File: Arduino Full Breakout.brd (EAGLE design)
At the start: 114.3 x 149.9 mm, 18 parts, among them J1 ARDUINO_R3_SHIELDUNO_R3_SHIEL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

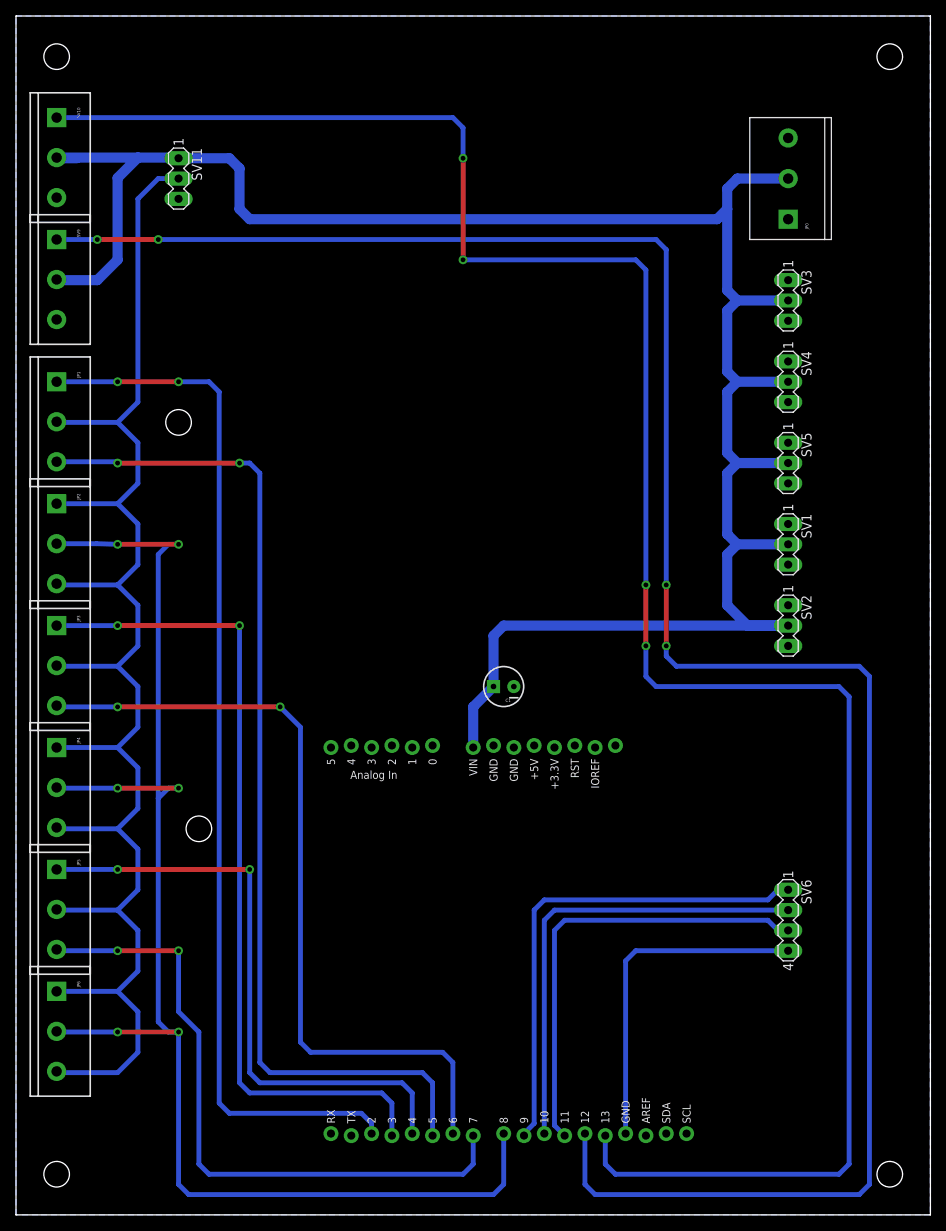
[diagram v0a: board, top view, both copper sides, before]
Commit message: add pushbutton debounce to full size breakout board
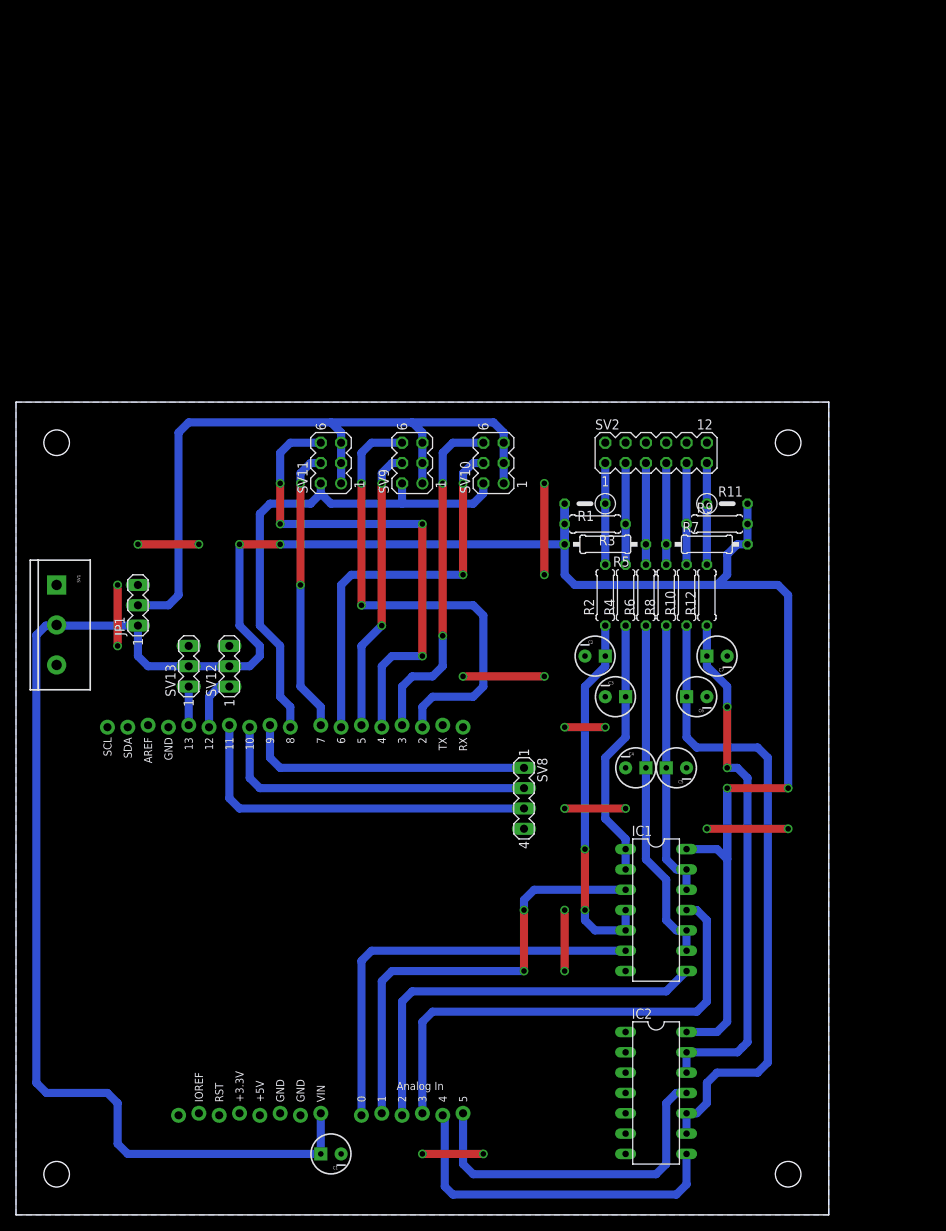
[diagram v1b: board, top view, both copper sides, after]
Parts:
- removed JP0: (no value), MY-Connectors:SCREWTERMINAL-5MM-3
- removed JP2, JP3, JP4, JP5, JP6: (no value), SparkFun-Connectors:SCREWTERMINAL-5MM-3
- removed SV3, SV4, SV5: (no value), con-lstb:MA03-1
- removed SV6: (no value), con-lstb:MA04-1
- added C2, C3, C4, C5, C6, C7: 10uF, SparkFun-Passives:CPOL-RADIAL-10UF-25V
- added IC1, IC2: 74HC00N, 74xx-eu:DIL14
- added R1, R11: 10k, rcl:0207/5V
- added R10, R12, R2, R4, R6, R8: 1k00, rcl:0207/7
- added R3, R9: 10k, rcl:0207/7
- added R5, R7: 10k, rcl:0207/10
- added SV12, SV13: (no value), con-lstb:MA03-1
- added SV8: (no value), con-lstb:MA04-1
- JP1: device SparkFun-Connectors:SCREWTERMINAL-5MM-3 -> con-lstb:MA03-1
- SV1: device con-lstb:MA03-1 -> SparkFun-Connectors:SCREWTERMINAL-5MM-3
- SV10, SV9: device SparkFun-Connectors:SCREWTERMINAL-5MM-3 -> con-lstb:MA03-2
- SV11: device con-lstb:MA03-1 -> con-lstb:MA03-2
- SV2: device con-lstb:MA03-1 -> con-lstb:MA06-2
- moved J1 108.2 mm to (1.27, 63.5), turned to 270 degrees
- moved SV1 91.6 mm to (5.08, 78.7)
- moved SV10 69.6 mm to (59.7, 94.0), turned to 90 degrees
- moved C1 62.3 mm to (39.4, 7.62)
- moved SV9 52.5 mm to (49.5, 94.0), turned to 90 degrees
- moved SV11 40.3 mm to (39.4, 94.0), turned to 90 degrees
- moved JP1 29.7 mm to (15.2, 76.2), turned to 90 degrees
- moved SV2 27.2 mm to (80.0, 95.2), turned to 0 degrees
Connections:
- removed net B0: SV1.1
- removed net B1: SV2.1
- removed net B2: SV3.1
- removed net B4: SV4.1
- removed net B5: SV5.1
- new net BUTTONS3: IC1.11, J1.A3
- new net N$10: C5.1, IC1.12, IC1.13, R8.1
- new net N$11: R7.1, R8.2, SV2.7
- new net N$12: C6.1, IC2.10, IC2.9, R10.1
- new net N$13: R10.2, R9.1, SV2.9
- new net N$16: C7.1, IC2.12, IC2.13, R12.1
- new net N$17: R11.1, R12.2, SV2.11
- new net N$3: C2.1, IC1.4, IC1.5, R2.1
- new net N$4: R1.1, R2.2, SV2.1
- new net N$5: C3.1, IC1.1, IC1.2, R4.1
- new net N$6: R3.1, R4.2, SV2.3
- new net N$7: C4.1, IC1.10, IC1.9, R6.1
- new net N$8: R5.1, R6.2, SV2.5
- net BUTTONS0: now also IC1.6
- net BUTTONS1: now also IC1.3
- net BUTTONS2: now also IC1.8
- net BUTTONS4: now also IC2.8
- net BUTTONS5: now also IC2.11
- net GND: now also C2.2, C3.2, C4.2, C5.2, C6.2, C7.2, IC1.7, IC2.1, IC2.2, IC2.4, IC2.5, IC2.7, JP1.3, SV12.3, SV13.3, SV2.10, SV2.12, SV2.2, SV2.4, SV2.6, SV2.8, SV8.4; no longer JP0.3, SV10.3, SV11.3, SV2.3, SV3.3, SV4.3, SV5.3, SV6.4, SV9.3
- net LIMITS0: now also SV8.1; no longer SV6.1
- net LIMITS1: now also SV8.2; no longer SV6.2
- net LIMITS2: now also SV8.3; no longer SV6.3
- net N$1: now also SV10.1, SV10.3, SV10.5, SV11.1, SV11.3, SV11.5, SV9.1, SV9.3, SV9.5; no longer JP2.1, JP2.3, JP3.2, JP4.1, JP4.3, JP5.2, JP6.1, JP6.3, SV11.2
- net SPINDLE0: now also SV12.1; no longer SV9.1
- net SPINDLE1: now also SV13.1; no longer SV10.1
- net STEP0: now also SV9.6; no longer JP1.1
- net STEP1: now also SV10.6; no longer JP3.1
- net STEP2: now also SV11.6; no longer JP5.1
- net STEP3: now also SV9.4; no longer JP1.3
- net STEP4: now also SV10.4; no longer JP3.3
- net STEP5: now also SV11.4; no longer JP5.3
- net STEP6: now also SV10.2, SV11.2, SV9.2; no longer JP2.2, JP4.2, JP6.2
- net VCC: now also IC1.14, IC2.14, JP1.1, R1.2, R11.2, R3.2, R5.2, R7.2, R9.2, SV12.2, SV13.2; no longer JP0.2, SV10.2, SV11.1, SV2.2, SV3.2, SV4.2, SV5.2, SV9.2
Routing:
- net SPINDLE1: track 262.0 -> 4.83 mm, vias 4 -> 0
- net SPINDLE0: track 260.4 -> 6.88 mm, vias 4 -> 0
- net STEP6: track 180.7 -> 63.4 mm, vias 6 -> 0
- net N$1: track 202.3 -> 90.3 mm
- net STEP3: track 128.9 -> 35.6 mm
- net N$12: track 0.00 -> 80.1 mm
- net STEP0: track 131.1 -> 60.5 mm
- net N$16: track 0.00 -> 65.6 mm, vias 0 -> 2
- net VCC: track 266.5 -> 328.8 mm, vias 0 -> 4
- net BUTTONS3: track 0.00 -> 61.3 mm
- net STEP1: track 104.2 -> 43.2 mm
- net BUTTONS1: track 0.00 -> 56.9 mm, vias 0 -> 2
- net BUTTONS0: track 0.00 -> 52.9 mm
- net BUTTONS2: track 0.00 -> 51.4 mm
- net STEP4: track 100.1 -> 49.3 mm
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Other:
- board size 114.3 x 149.9 mm -> 101.6 x 101.6 mm
